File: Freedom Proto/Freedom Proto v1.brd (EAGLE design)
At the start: 100 x 100 mm, 8 parts, among them X1 0446200002

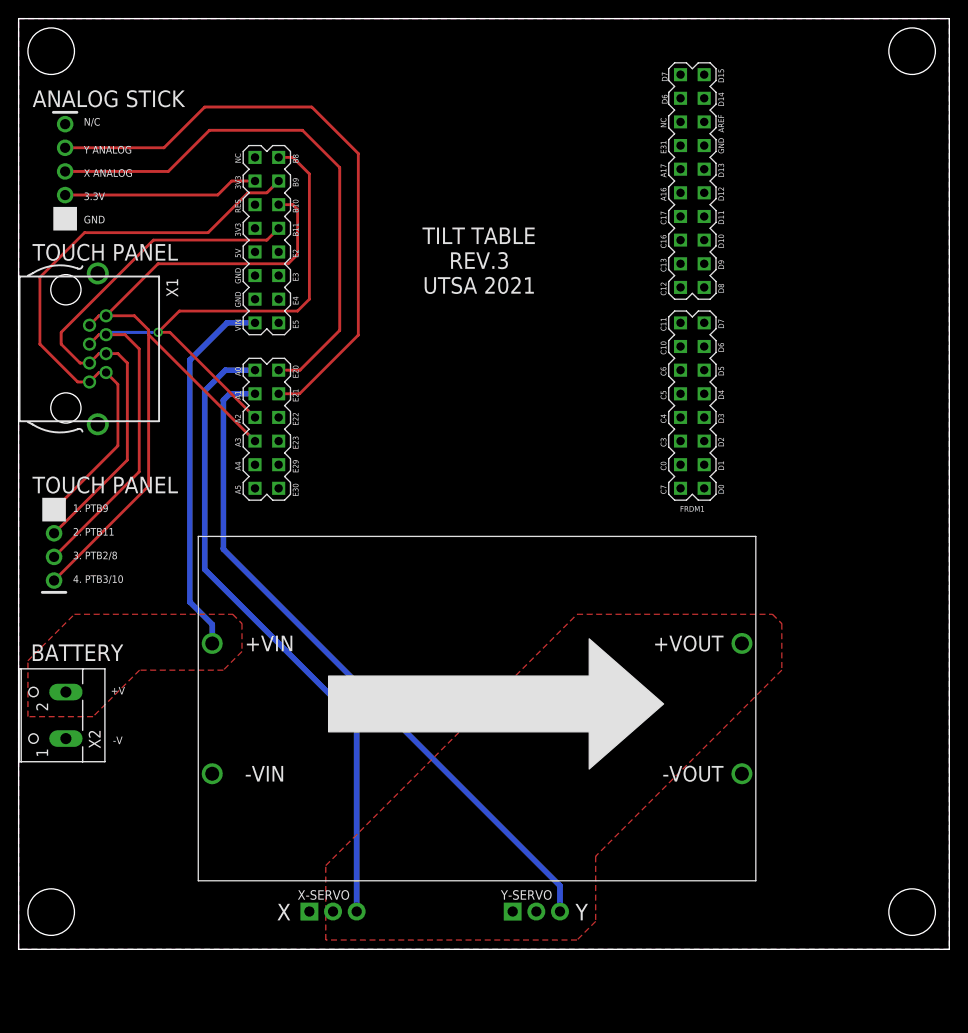
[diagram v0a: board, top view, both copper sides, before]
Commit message: ATmega328 reference design
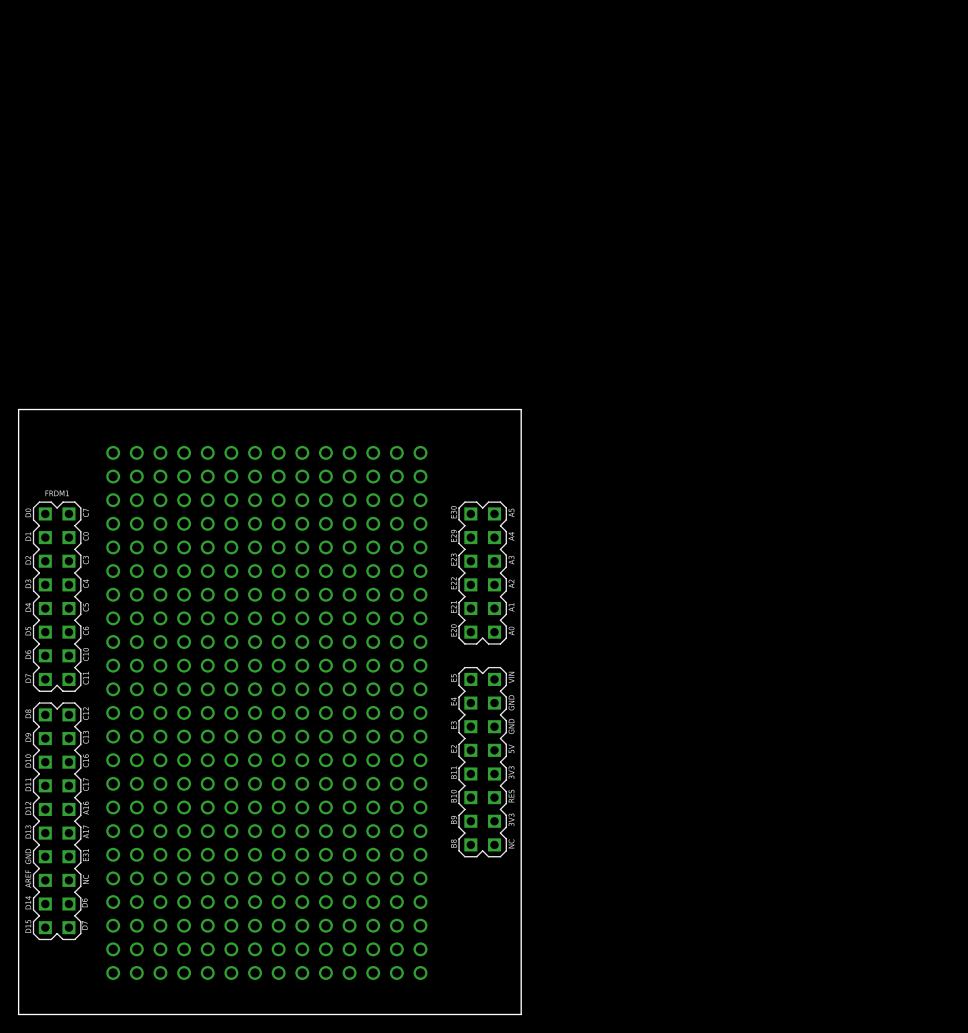
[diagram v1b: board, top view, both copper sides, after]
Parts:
- removed JS: PINS_5SILK, nolan-utsa:PCB_5
- removed U$3: PINS_4SILK, nolan-utsa:PCB_4
- removed U$4: MODULE-DCDC, nolan-utsa:DCDC_CONVERTER_MH
- removed X-SERVO, Y-SERVO: PINS_3_2.54, nolan-utsa:PINS_3
- removed X1: 0446200002, con-molex:0446200002
- removed X2: (no value), con-wago-500:W237-102
- moved FRDM1 44.4 mm to (27.0, 29.0), turned to 0 degrees
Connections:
- removed net 3.3V: FRDM1.3V3, JS.P$2
- removed net 5-9V: FRDM1.VIN, U$4.+VIN, X2.2
- removed net BLU: FRDM1.PTB11, U$3.P$2, X1.3, X1.4
- removed net BRN: FRDM1.A3, FRDM1.PTB10, U$3.P$4, X1.7, X1.8
- removed net GND: FRDM1.GND0, FRDM1.GND1, FRDM1.GND2, JS.P$1, U$4.-VIN, U$4.-VOUT, X-SERVO.1, X1.S@1, X1.S@2, X2.1, Y-SERVO.1
- removed net GRN: FRDM1.A2, FRDM1.PTB8, U$3.P$3, X1.5, X1.6
- removed net N$2: U$4.+VOUT, X-SERVO.2, Y-SERVO.2
- removed net ORG: FRDM1.PTB9, U$3.P$1, X1.1, X1.2
- removed net PTB0: FRDM1.A0, X-SERVO.3
- removed net PTB1: FRDM1.A1, Y-SERVO.3
- removed net X_ANA: FRDM1.PTE20, JS.P$3
- removed net Y_ANA: FRDM1.PTE21, JS.P$4
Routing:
- net GRN: track 88.2 -> 0.00 mm, vias 1 -> 0
- net BRN: track 85.1 -> 0.00 mm
- net PTB1: track 73.6 -> 0.00 mm
- net PTB0: track 69.0 -> 0.00 mm
- net Y_ANA: track 66.1 -> 0.00 mm
- net ORG: track 64.4 -> 0.00 mm
- net BLU: track 59.6 -> 0.00 mm
- net X_ANA: track 58.8 -> 0.00 mm
- net 5-9V: track 40.1 -> 0.00 mm
- net 3.3V: track 21.0 -> 0.00 mm
- removed copper zone on layer 1, net 5-9V
- removed copper zone on layer 1, net GND
- removed copper zone on layer 16, net GND
- removed copper zone on layer 1, net N$2
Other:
- board size 100 x 100 mm -> 54 x 65 mm
- board text removed: "+V"
- board text removed: "-V"
- board text removed: "1. PTB9"
- board text removed: "2. PTB11"
- board text removed: "3. PTB2/8"
- board text removed: "3.3V"
- board text removed: "4. PTB3/10"
- board text removed: "ANALOG STICK"
- board text removed: "BATTERY"
- board text removed: "GND"
- board text removed: "N/C"
- board text removed: "TILT TABLE REV.3 UTSA 2021"
- board text removed: "TOUCH PANEL"
- board text removed: "X"
- board text removed: "X ANALOG"
- board text removed: "Y"
- board text removed: "Y ANALOG"
